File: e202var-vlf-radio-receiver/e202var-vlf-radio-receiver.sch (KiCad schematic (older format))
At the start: 49 parts, among them J1 9V, J2 ON/OFF, J3 HEADPHONES, J4 12V/18V, Q1 BC547, Q2 BC547, U1 MC7809, U2 TLE2426, U3 NJM386, U4 TL081CP

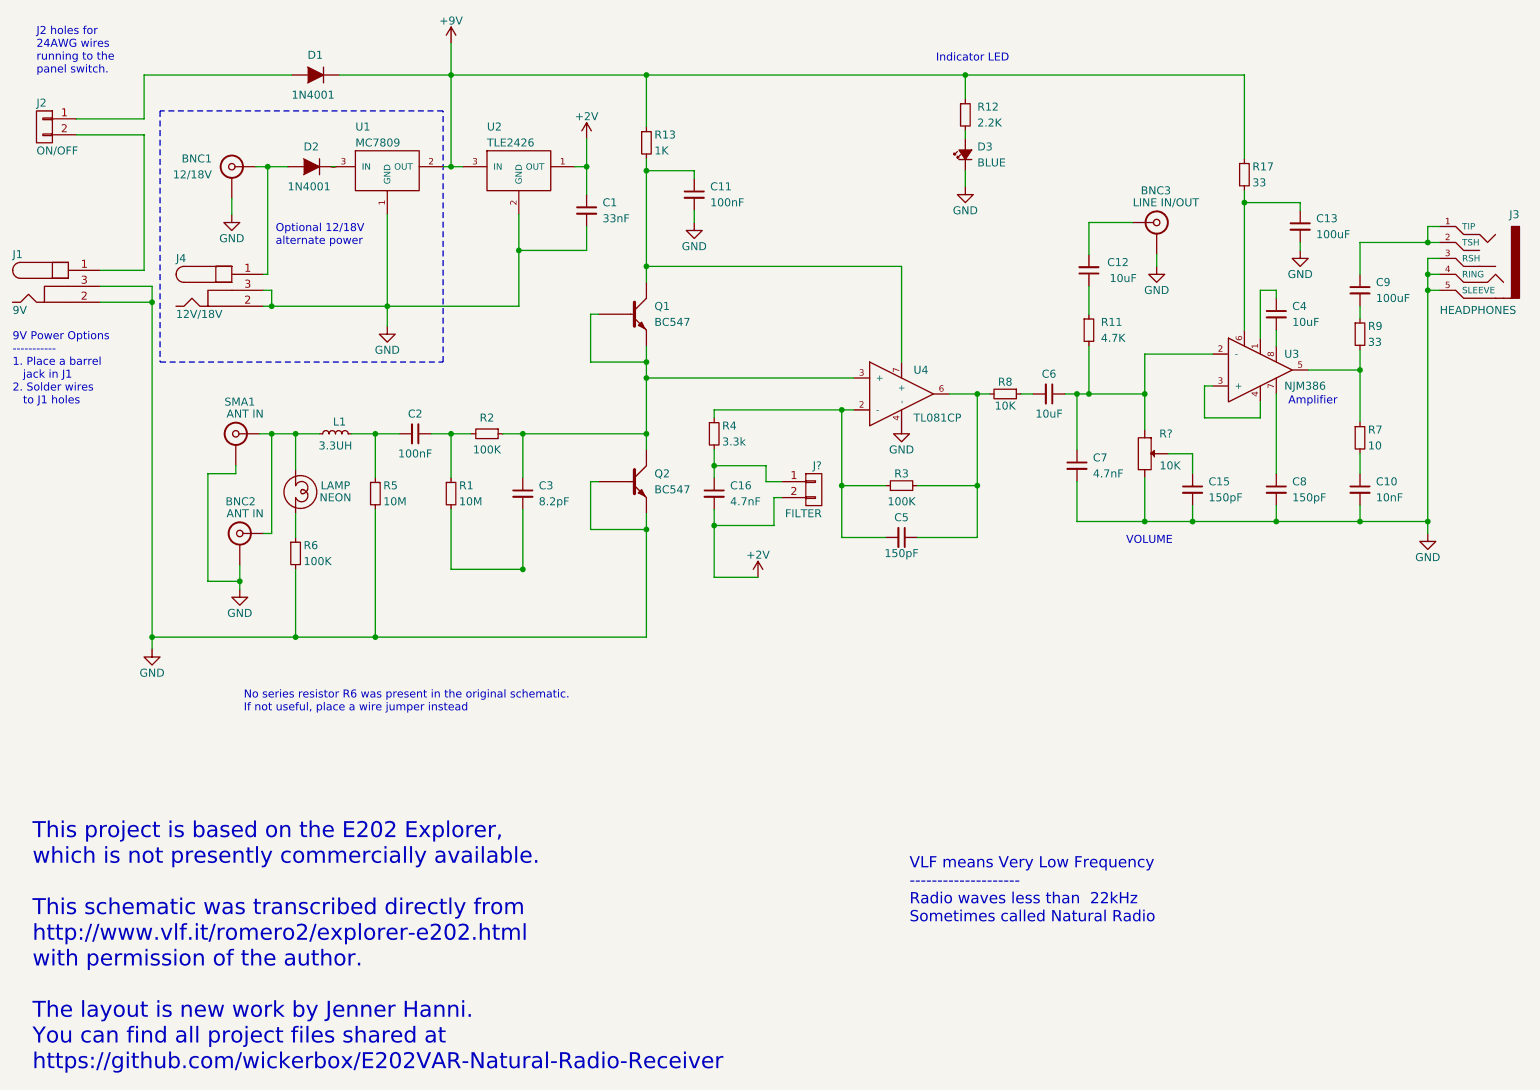
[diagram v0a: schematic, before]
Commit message: Rough part placement. Created README. Images made by gerbv are off-center.
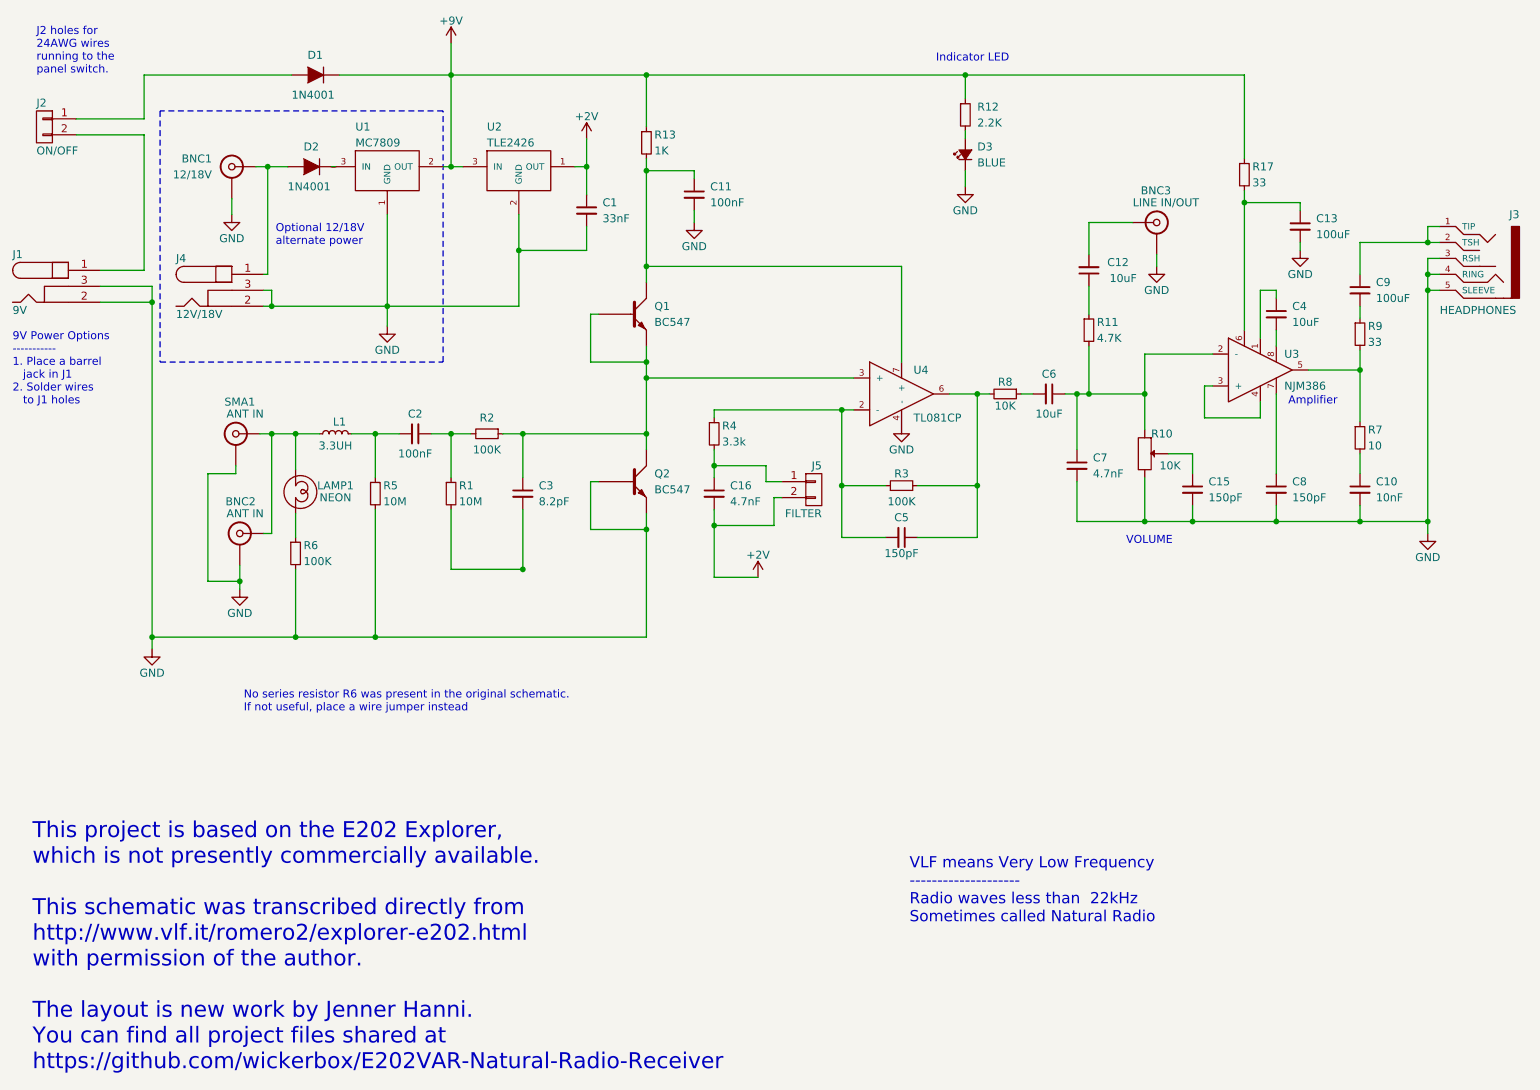
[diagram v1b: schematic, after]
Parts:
- removed R11: 4.7K, RLC-0402-SMD, symbol RES-4.7K-1%-1/10W-0402
- added R11: 4.7K, Wickerlib:RES-CARBONFILM-7MM, symbol RES-4.7K-5%-1/4W-TH-CFMINI
- J1, J4: footprint PJ-202BH -> Wickerlib:CONN-BARREL-JACK-2.5x5.5MM-TH
- J3: footprint SJ1-3523N -> Wickerlib:SJ1-3523N
- R13, R8: footprint CFM14 -> Wickerlib:RES-CARBONFILM-7MM
- R17, R9: footprint CF14 -> Wickerlib:RES-CARBONFILM-7MM
- U1: footprint TO220AB -> Wickerlib:TO-220-NEUTRAL123-VERT-LONGPADS
- gave numbers to parts that had none: 2
- renumbered LAMP to LAMP1
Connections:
- net at C6.1, C7.1, R10.1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: now also R11.2
- net at C12.1: now also R11.1
